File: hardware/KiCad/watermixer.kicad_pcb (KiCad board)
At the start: 2 copper layers, 144.8 x 100 mm, 21 parts, among them U1 Display, U2 ESP32-DevKitC, U3 LLC_4CH, U4 MCP4728

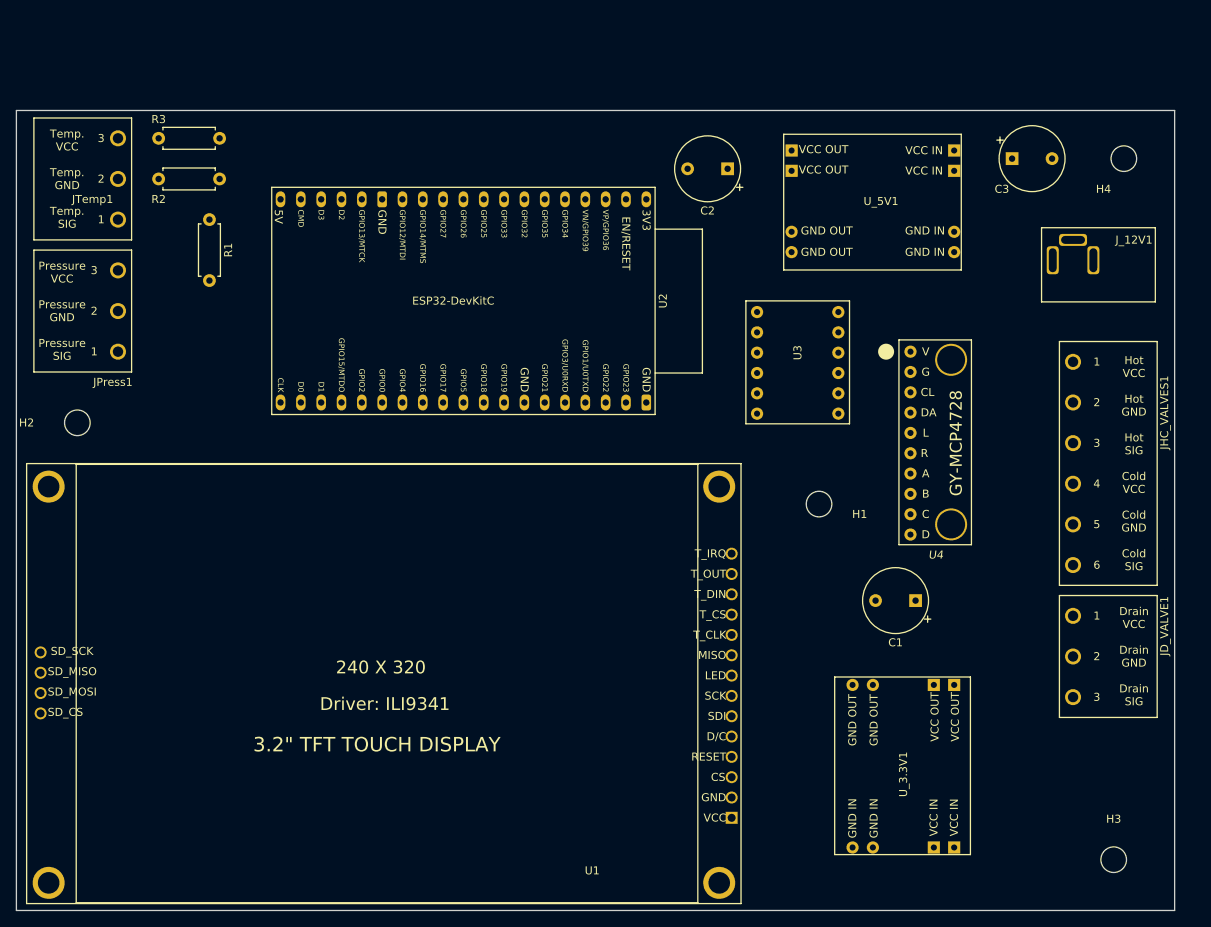
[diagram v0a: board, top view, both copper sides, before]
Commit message: Connected all on PCB except GND
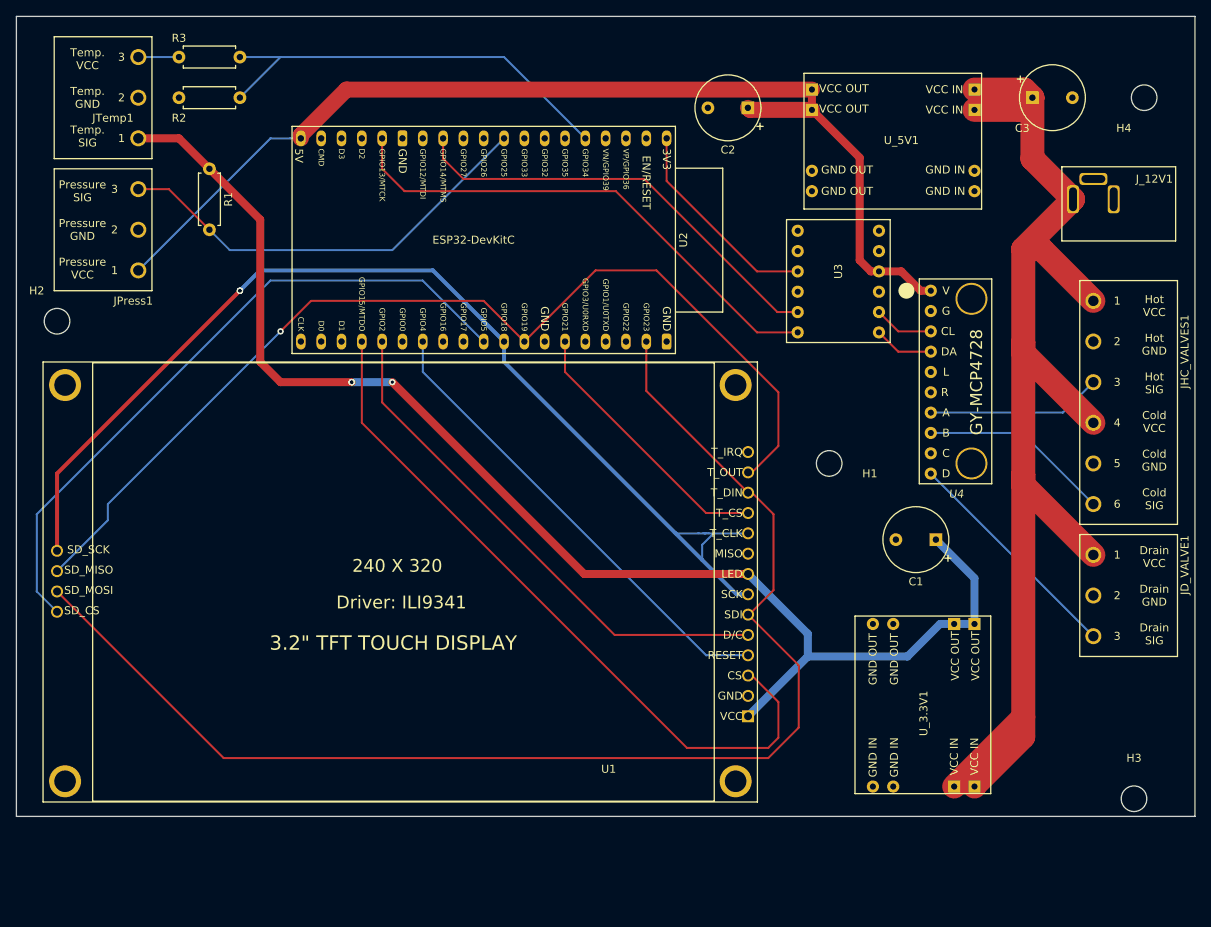
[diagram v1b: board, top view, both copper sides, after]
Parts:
- U1: value Display -> CR2013-MI2120-touch
- moved H2 13.0 mm to (76.2, 63.5)
- moved U1 12.9 mm to (163.3, 113.0)
- moved U3 11.4 mm to (180.3, 50.8)
- moved JTemp1 10.5 mm to (86.4, 43.2)
- moved JPress1 10.5 mm to (86.4, 59.7)
- moved R3 10.5 mm to (91.4, 30.5)
- moved R2 10.5 mm to (91.4, 35.6)
- moved JD_VALVE1 8.03 mm to (205.7, 90.2)
- moved JHC_VALVES1 8.03 mm to (205.7, 58.4)
- moved U_3.3V1 8.03 mm to (175.9, 122.6)
- moved U_5V1 8.03 mm to (191.8, 49.5)
- moved C2 8.03 mm to (162.6, 36.8)
- moved H3 8.03 mm to (210.8, 123.2)
- moved C1 8.03 mm to (186.1, 90.8)
- moved C3 8.03 mm to (198.1, 35.6)
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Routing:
- net VDD: track 0.00 -> 168.2 mm, vias 0 -> 3
- net Net-(U1-Pad11): track 0.00 -> 161.3 mm
- net VCC: track 0.00 -> 159.8 mm
- net Net-(U1-Pad13): track 0.00 -> 138.1 mm, vias 0 -> 2
- net VDDF: track 0.00 -> 136.2 mm
- net Net-(U1-Pad12): track 0.00 -> 129.0 mm, vias 0 -> 1
- net Net-(U1-Pad3): track 0.00 -> 88.7 mm
- net Net-(U1-Pad10): track 0.00 -> 84.4 mm
- net Net-(U1-Pad5): track 0.00 -> 65.9 mm
- net Net-(U2-Pad15): track 0.00 -> 64.2 mm
- net /SIG: track 0.00 -> 59.7 mm
- net Net-(U1-Pad4): track 0.00 -> 59.1 mm
- net Net-(U2-Pad12): track 0.00 -> 54.8 mm
- net Net-(R2-Pad2): track 0.00 -> 54.6 mm
- net Net-(U1-Pad15): track 0.00 -> 34.0 mm
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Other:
- board size 144.8 x 100 mm -> 147.3 x 100 mm
- board text added: "Pressure SIG Pressure GND Pressure VCC"
- board text removed: "Pressure VCC Pressure GND Pressure SIG"

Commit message: before grounding
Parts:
- moved H2 43.6 mm to (106.7, 32.4)
- moved H3 7.85 mm to (208.9, 115.6)
- moved R2 2.54 mm to (88.9, 35.6)
- moved R3 2.54 mm to (88.9, 30.5)
- moved JPress1 1.91 mm to (84.5, 59.7)
- moved JTemp1 1.91 mm to (84.5, 43.2)
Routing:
- net Net-(R2-Pad2): track 54.6 -> 68.5 mm
- net GND: track 0.00 -> 4.45 mm
- net VDD: track 168.2 -> 170.1 mm
- net /SIG: track 59.7 -> 61.0 mm

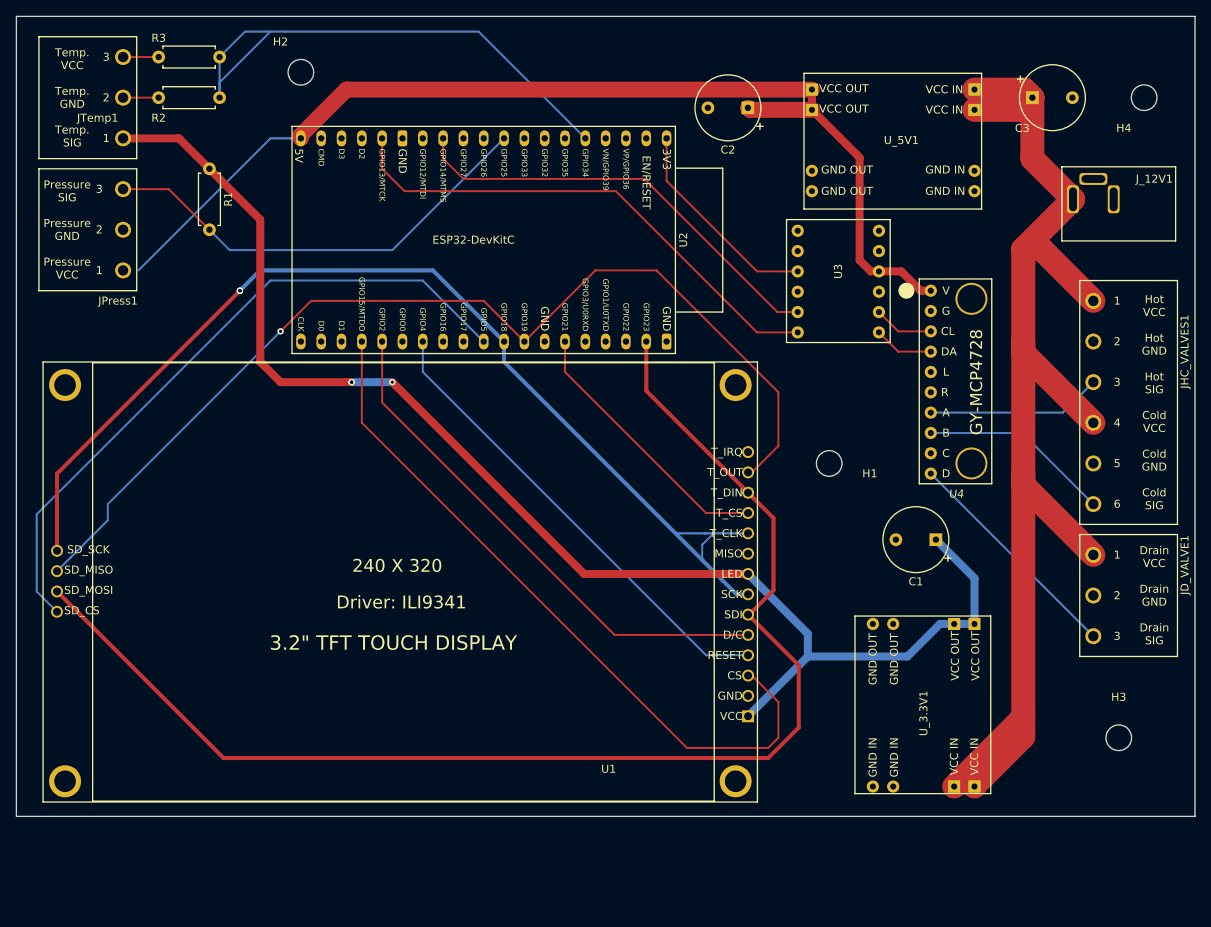
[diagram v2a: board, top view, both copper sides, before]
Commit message: added GND fill zones on top and bottom layers
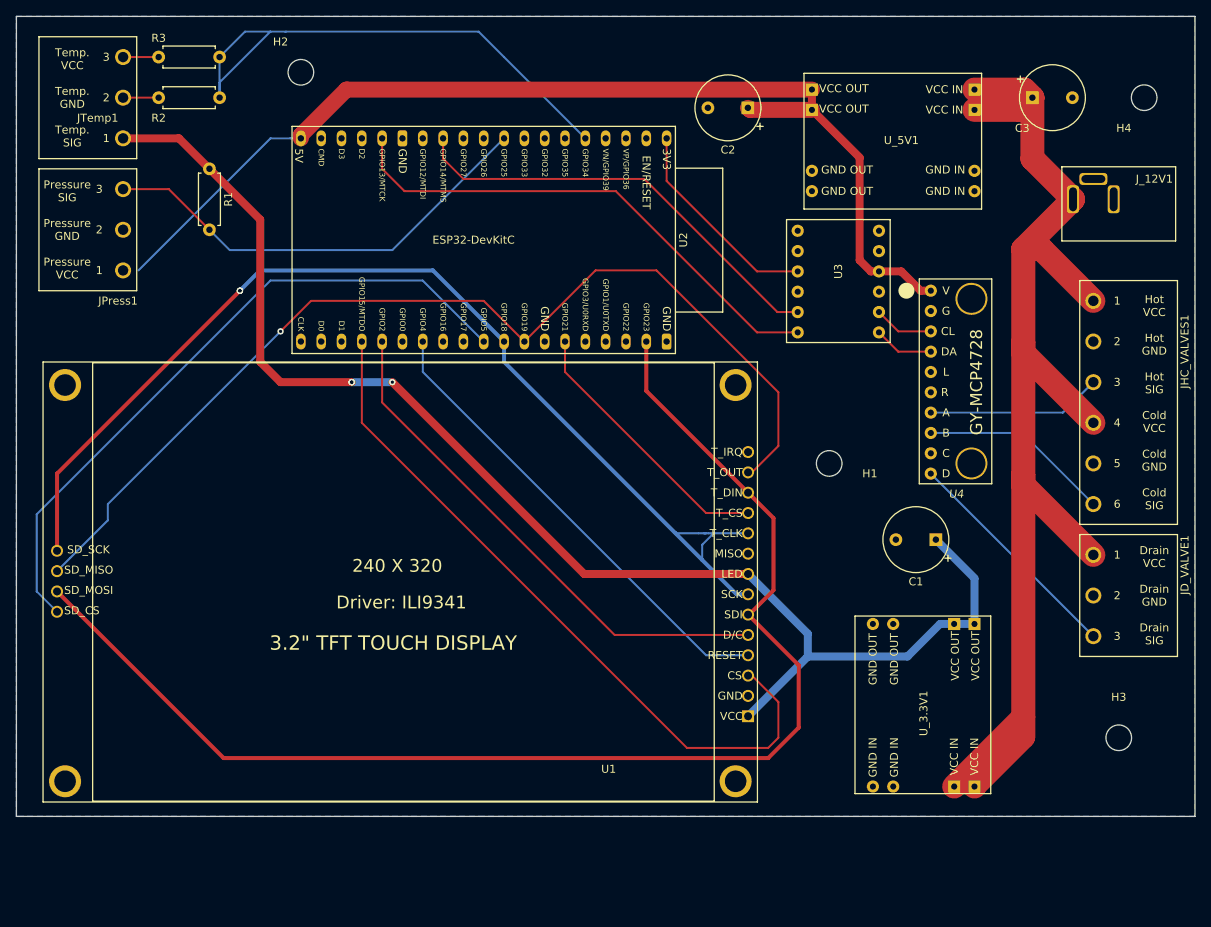
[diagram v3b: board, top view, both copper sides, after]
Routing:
- added copper zone on B.Cu, net GND
